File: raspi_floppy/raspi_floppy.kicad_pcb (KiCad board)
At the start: 2 copper layers, 137.2 x 78.7 mm, 22 parts, among them J1 Raspberry_Pi_2_3, J5 Conn_02x17_Odd_Even, U1 74LS06, U2 74LS06

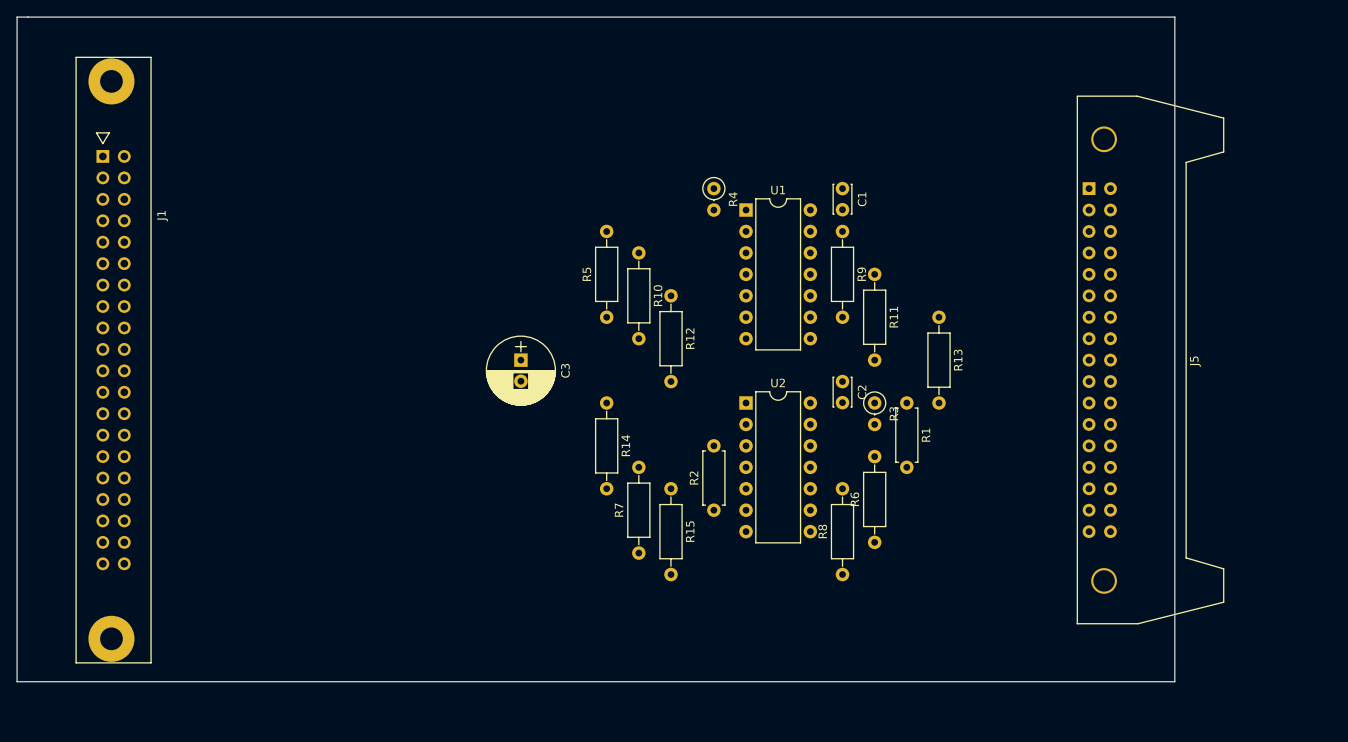
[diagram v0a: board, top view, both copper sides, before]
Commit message: Update Pi floppy i/f.
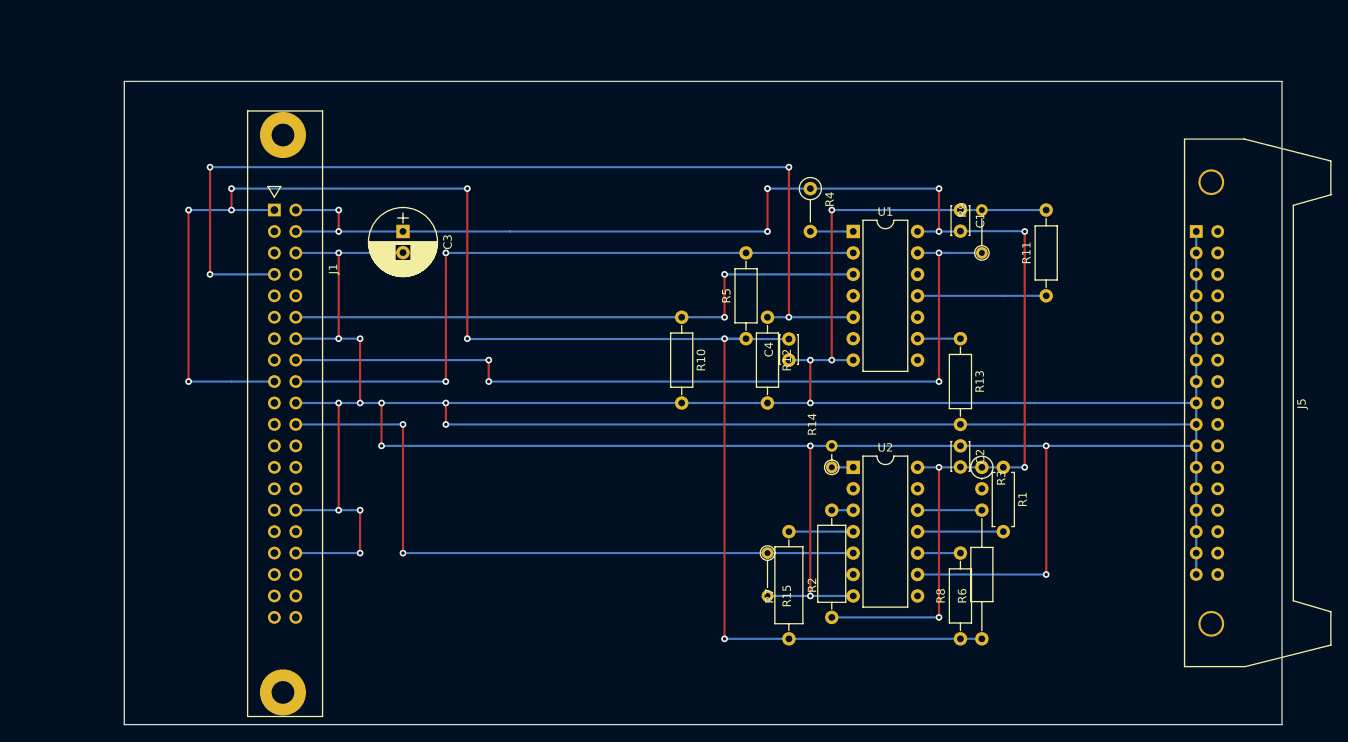
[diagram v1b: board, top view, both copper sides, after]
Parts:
- added C4: 0u1, Capacitors_ThroughHole:C_Disc_D3.4mm_W2.1mm_P2.50mm, F.Cu at (167.6, 96.5)
- R14: footprint Resistors_ThroughHole:R_Axial_DIN0207_L6.3mm_D2.5mm_P10.16mm_Horizontal -> Resistors_ThroughHole:R_Axial_DIN0204_L3.6mm_D1.6mm_P2.54mm_Vertical
- R15, R9: footprint Resistors_ThroughHole:R_Axial_DIN0207_L6.3mm_D2.5mm_P10.16mm_Horizontal -> Resistors_ThroughHole:R_Axial_DIN0204_L3.6mm_D1.6mm_P5.08mm_Vertical
- R2: footprint Resistors_ThroughHole:R_Axial_DIN0207_L6.3mm_D2.5mm_P7.62mm_Horizontal -> Resistors_ThroughHole:R_Axial_DIN0309_L9.0mm_D3.2mm_P12.70mm_Horizontal
- R4: footprint Resistors_ThroughHole:R_Axial_DIN0207_L6.3mm_D2.5mm_P2.54mm_Vertical -> Resistors_ThroughHole:R_Axial_DIN0207_L6.3mm_D2.5mm_P5.08mm_Vertical
- R6: footprint Resistors_ThroughHole:R_Axial_DIN0207_L6.3mm_D2.5mm_P10.16mm_Horizontal -> Resistors_ThroughHole:R_Axial_DIN0207_L6.3mm_D2.5mm_P15.24mm_Horizontal
- R7: footprint Resistors_ThroughHole:R_Axial_DIN0207_L6.3mm_D2.5mm_P10.16mm_Horizontal -> Resistors_ThroughHole:R_Axial_DIN0309_L9.0mm_D3.2mm_P12.70mm_Horizontal
- moved R14 27.7 mm to (172.7, 109.2), turned to 90 degrees
- moved J1 21.3 mm to (106.7, 78.7)
- moved C3 20.7 mm to (121.9, 81.3)
- moved R11 20.5 mm to (198.1, 88.9), turned to 90 degrees
- moved R7 20.5 mm to (167.6, 129.5)
- moved R2 18.9 mm to (172.7, 127.0)
- moved R6 17.1 mm to (190.5, 129.5)
- moved R5 16.7 mm to (162.6, 94.0)
- moved R9 16.7 mm to (190.5, 83.8), turned to 90 degrees
- moved C2 15.9 mm to (188.0, 106.7)
- moved R8 15.9 mm to (188.0, 129.5)
- moved R3 14.8 mm to (190.5, 109.2)
- moved U2 14.8 mm to (175.3, 109.2)
- moved C1 14.2 mm to (188.0, 78.7)
- moved R15 13.7 mm to (165.1, 119.4)
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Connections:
- J1 pad 3: /PI_WE -> /PI_WR_EN
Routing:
- net GND: track 0.00 -> 525.8 mm, vias 0 -> 20
- net +3V3: track 0.00 -> 195.6 mm, vias 0 -> 8
- net +5V: track 0.00 -> 177.9 mm, vias 0 -> 10
- net /PI_SEEK: track 0.00 -> 116.8 mm, vias 0 -> 4
- net /PI_DRV_SEL: track 0.00 -> 102.9 mm, vias 0 -> 4
- net /PI_INDEX: track 0.00 -> 81.3 mm, vias 0 -> 2
- net /PI_SIDE_SEL: track 0.00 -> 81.3 mm, vias 0 -> 2
- net /PI_LOAD: track 0.00 -> 71.1 mm, vias 0 -> 2
- net /PI_DIR: track 0.00 -> 15.2 mm
- net /RD_DATA: track 0.00 -> 10.2 mm
- net /PI_WR_PROT: track 0.00 -> 7.62 mm
- net /PI_TRACK0: track 0.00 -> 7.62 mm
- net /PI_WR_DATA: track 0.00 -> 5.08 mm
- net /PI_RD_DATA: track 0.00 -> 5.08 mm
- net /INDEX: track 0.00 -> 5.08 mm
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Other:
- board size 137.2 x 78.7 mm -> 137.2 x 76.2 mm
